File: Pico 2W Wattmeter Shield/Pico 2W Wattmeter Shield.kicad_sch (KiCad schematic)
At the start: 23 parts, among them J1 RF In, J2 Socket_1x20_P2.54mm, J3 Socket_1x20_P2.54mm, U1 ADL5904, U2 ADS1115IDGS

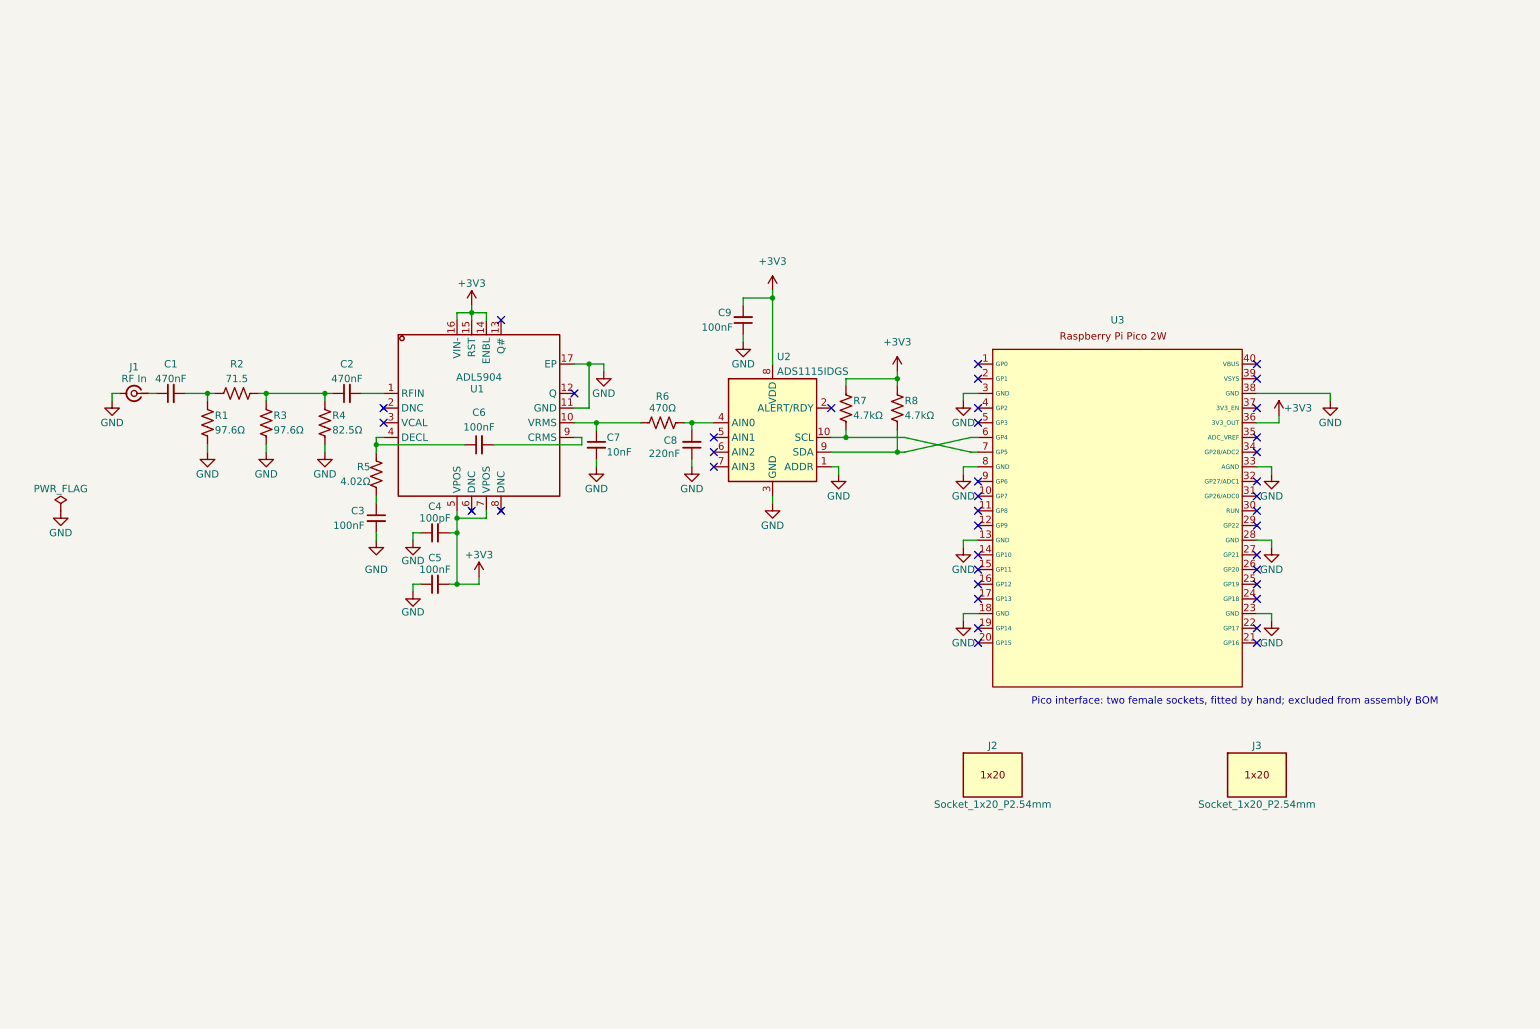
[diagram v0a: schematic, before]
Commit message: Updated wattmeter design
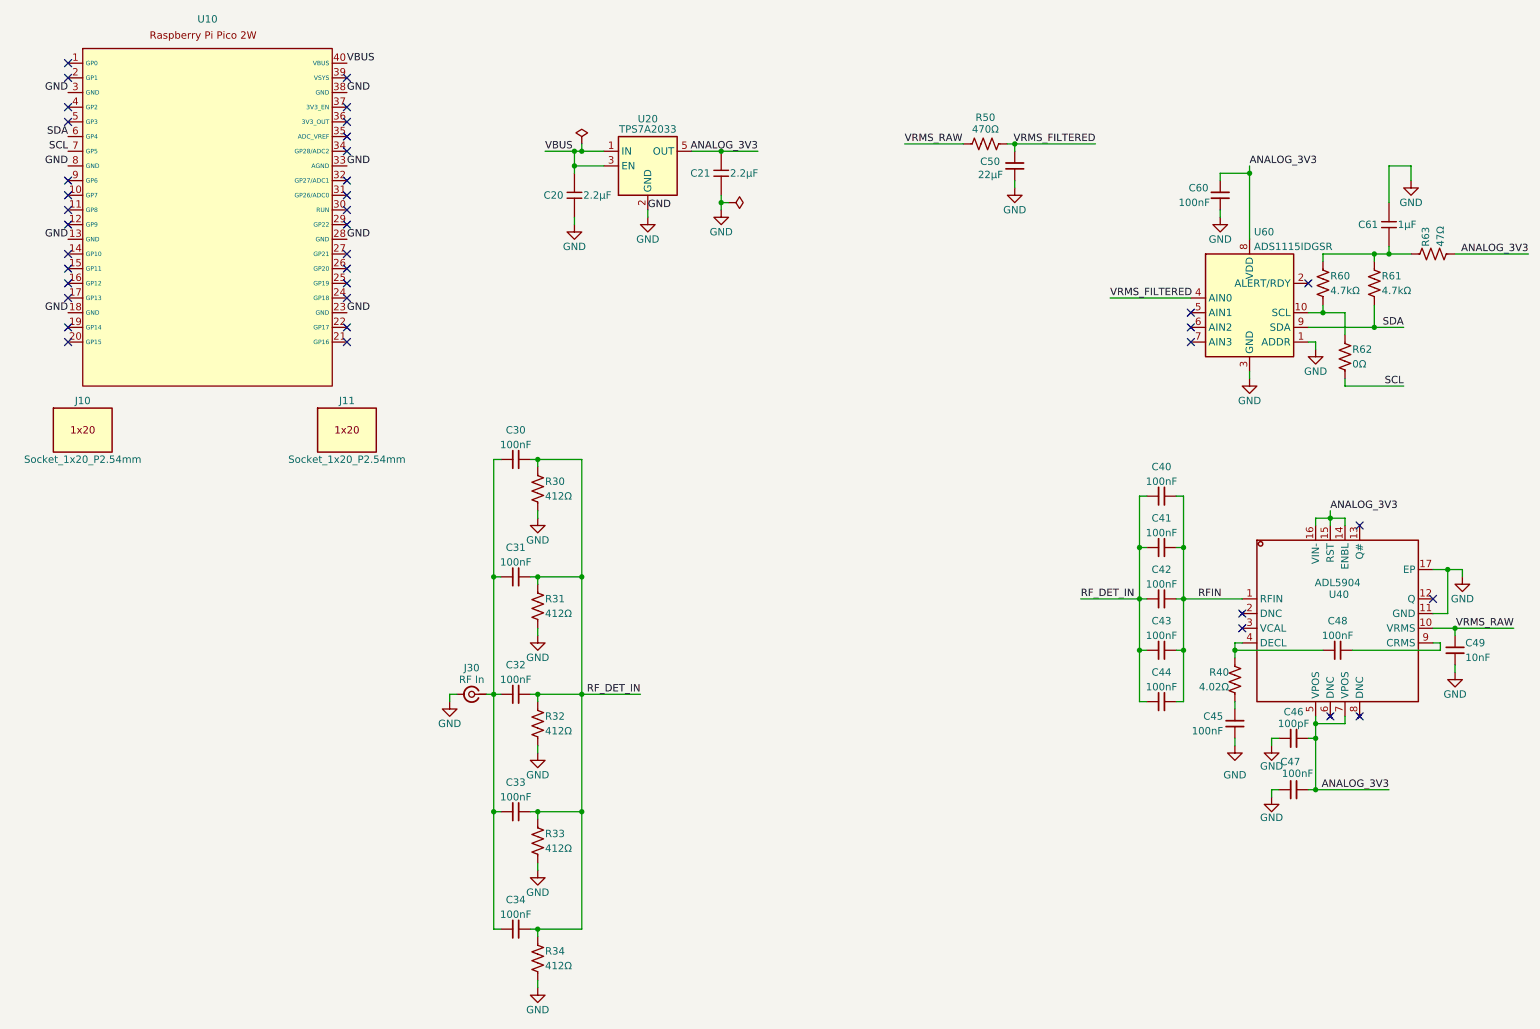
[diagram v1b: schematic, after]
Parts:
- removed C1, C2: 470nF, pico-wattmeter:C_0402_1005Metric, symbol Device:C_Small
- removed C5, C6: 100nF, pico-wattmeter:C_0402_1005Metric, symbol Device:C_Small
- removed R1, R3: 97.6Ω, pico-wattmeter:R_0805_2012Metric, symbol Device:R_US
- removed R2: 71.5, pico-wattmeter:R_0805_2012Metric, symbol Device:R_US
- removed R4: 82.5Ω, pico-wattmeter:R_0402_1005Metric, symbol Device:R_US
- added C20, C21: 2.2μF, pico-wattmeter:C_0805_2012Metric, symbol pico-wattmeter:C
- added C30, C31, C32, C33, C34, C40, C41, C42, C43, C44, C48: 100nF, pico-wattmeter:C_1206_3216Metric, symbol Device:C_Small
- added C47: 100nF, pico-wattmeter:C_0402_1005Metric, symbol Device:C_Small
- added C61: 1μF, pico-wattmeter:C_0603_1608Metric, symbol pico-wattmeter:C
- added R30, R31, R32, R33, R34: 412Ω, pico-wattmeter:R_0402_1005Metric, symbol Device:R_US
- added R62: 0Ω, pico-wattmeter:R_0805_2012Metric, symbol Device:R_US
- added R63: 47Ω, pico-wattmeter:R_0402_1005Metric, symbol Device:R_US
- added U20: TPS7A2033, pico-wattmeter:SOT-23-5, symbol pico-wattmeter:TPS7A2033PDBVR
- C45: renamed from C3; LCSC Part # C60474 -> C1525; MPN (none) -> CL05B104KO5NNNC; Manufacturer (none) -> Samsung Electro-Mechanics
- C46: renamed from C4; MPN (none) -> 0402CG101J500NT; Manufacturer (none) -> FH
- C49: renamed from C7; LCSC Part # C85735 -> C15195; MPN (none) -> CL05B103KB5NNNC; Manufacturer (none) -> Samsung Electro-Mechanics
- C50: renamed from C8; value 220nF -> 22µF; footprint pico-wattmeter:C_0402_1005Metric -> pico-wattmeter:C_0805_2012Metric; LCSC Part # C16772 -> C602037; MPN (none) -> CL21A226MAYNNNE; Manufacturer (none) -> Samsung Electro-Mechanics
- C60: renamed from C9; LCSC Part # C60474 -> C1525; MPN (none) -> CL05B104KO5NNNC; Manufacturer (none) -> Samsung Electro-Mechanics
- R40: renamed from R5; MPN (none) -> FRC0402F4R02TS; Manufacturer (none) -> FOJAN; Supplier URL (none) -> https://www.lcsc.com/product-detail/C55174786.html
- R50: renamed from R6; MPN (none) -> FRC0402F4700TS; Manufacturer (none) -> FOJAN
- R60: renamed from R7; MPN (none) -> 0402WGF4701TCE; Manufacturer (none) -> UNI-ROYAL; Supplier URL (none) -> https://www.lcsc.com/product-detail/C25900.html
- R61: renamed from R8; MPN (none) -> 0402WGF4701TCE; Manufacturer (none) -> UNI-ROYAL; Supplier URL (none) -> https://www.lcsc.com/product-detail/C25900.html
- U40: renamed from U1; MPN (none) -> ADL5904ACPZN-R7; Manufacturer (none) -> Analog Devices; Supplier URL (none) -> https://www.lcsc.com/product-detail/C206813.html
- U60: renamed from U2; value ADS1115IDGS -> ADS1115IDGSR; LCSC Part # C468683 -> C37593; MPN (none) -> ADS1115IDGSR; Manufacturer (none) -> Texas Instruments
- renumbered J2 to J10, J3 to J11, J1 to J30, U3 to U10
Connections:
- net GND: now also C20.2, C21.2, C47.2, C61.1, R30.2, R31.2, R32.2, R33.2, R34.2, U20.2 (GND)
- net at R40.1, U40.4 (DECL): now also C48.1
- net at J30.1 (In): now also C30.1, C31.1, C32.1, C33.1, C34.1
- net VRMS_FILTERED: now reaches C50.2, R50.2, U60.4 (AIN0)
- net VRMS_RAW: now reaches C49.1, R50.1, U40.10 (VRMS)
- net VBUS: now reaches U10.40 (VBUS)
- net VBUS: now also C20.1, U20.1 (IN), U20.3 (EN)
- net SDA: now reaches R61.2, U10.6 (GP4), U60.9 (SDA)
- net at R60.2, U60.10 (SCL): now also R62.1; no longer U10.7 (GP5)
- net RFIN: now reaches U40.1 (RFIN)
- net RFIN: now also C40.2, C41.2, C42.2, C43.2, C44.2
- net at U40.9 (CRMS): now also C48.2
- net +3V3 renamed ANALOG_3V3
- net ANALOG_3V3: now also C21.1, C47.1, R63.2, U20.5 (OUT); no longer R60.1, R61.1, U10.36 (3V3_OUT)
- new net: C61.2, R60.1, R61.1, R63.1
- new net RF_DET_IN: C30.2, C31.2, C32.2, C33.2, C34.2, C40.1, C41.1, C42.1, C43.1, C44.1, R30.1, R31.1, R32.1, R33.1, R34.1
- new net SCL: R62.2, U10.7 (GP5)
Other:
- note removed: "Pico interface: two female sockets, fitted by hand; excluded from assembly BOM"
- moved on the sheet: C45, C46, C49, C50, C60, J10, J11, J30, R40, R50, R60, R61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
